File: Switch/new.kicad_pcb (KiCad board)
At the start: 2 copper layers, 53.5 x 53 mm, 9 parts, among them J1 RJ45, J2 RJ45, J3 RJ45, J4 RJ45, SW1 Driver/Auton, SW2 Enable/Disable, SW3 Pin7, SW4 Pin4, SW5 Pin1

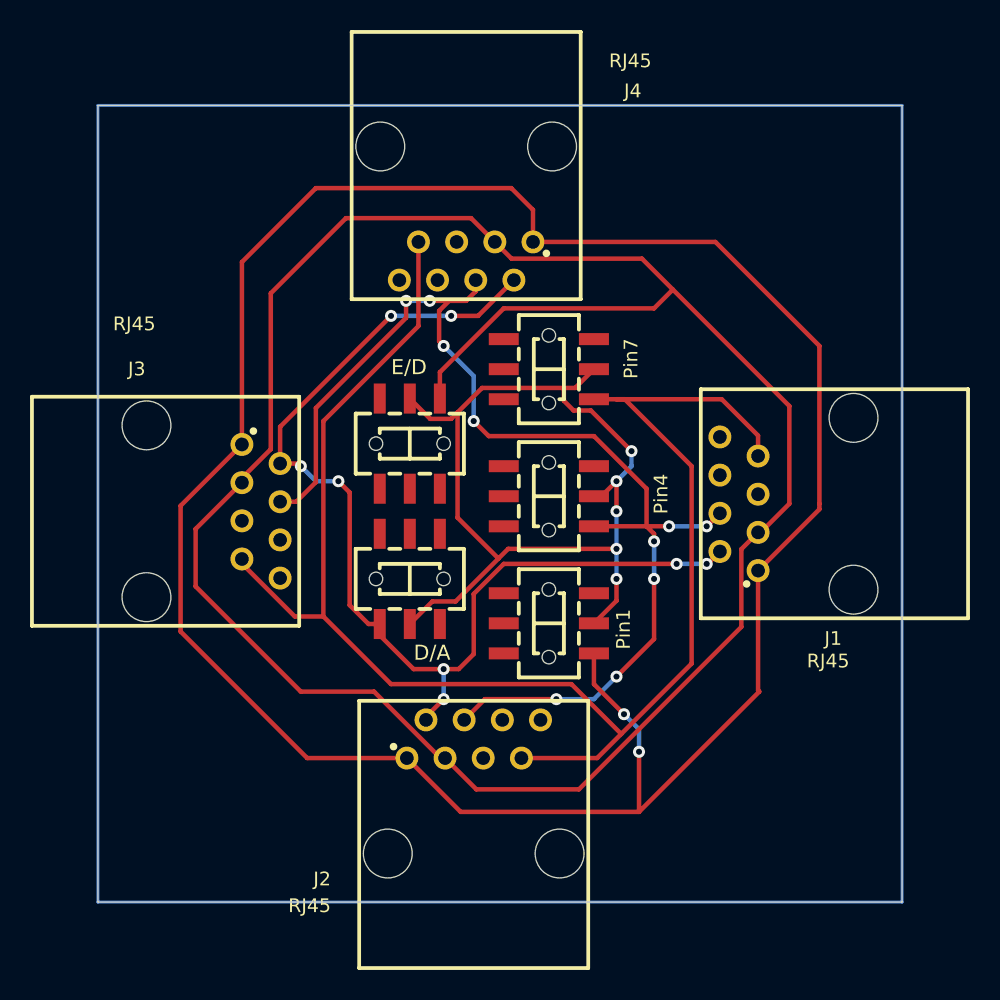
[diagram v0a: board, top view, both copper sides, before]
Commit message: switch with all files found in the folder
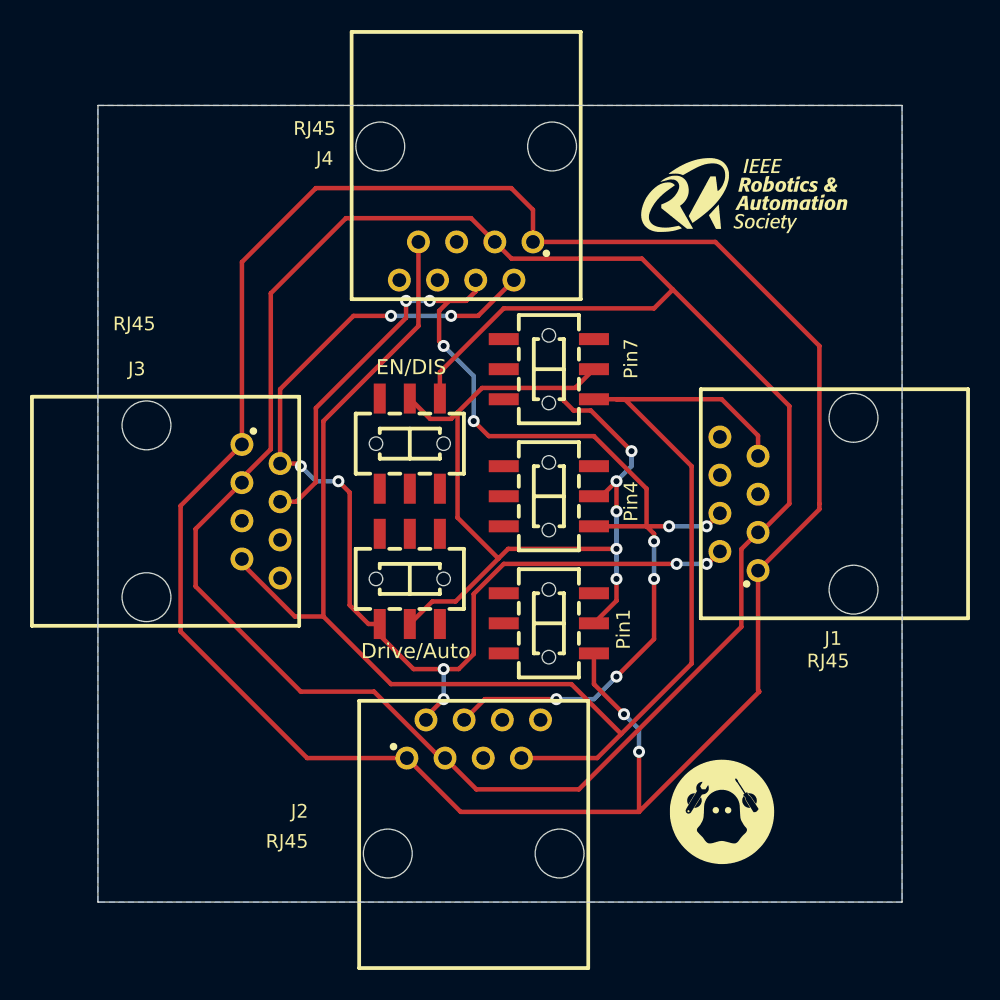
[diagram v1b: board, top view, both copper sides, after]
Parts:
- added G***: LOGO, ghost:ghost, F.Cu at (175.0, 106.5)
- added G***: LOGO, ghost:ieee, F.Cu at (176.5, 65.5)
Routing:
- net Net-(J1-Pad2): track 71.3 -> 72.7 mm
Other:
- board text added: "Drive/Auto"
- board text added: "EN/DIS"
- board text removed: "D/A"
- board text removed: "E/D"

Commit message: finalize comp switch
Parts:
- added G***: LOGO, ghost:ieee, B.Cu at (160.4, 77.4)
- added G***: LOGO, ghost:ghost, B.Cu at (160.5, 93.0)
- J1, J2, J3, J4: footprint RJ45Connector:RJ45-TH_RC0139 -> ghost:RJ45-TH_RC0139
- SW1, SW2, SW3, SW4, SW5: footprint Library:SW-SMD_MS-22D28-G020 -> ghost:SW-SMD_MS-22D28-G020
- moved G*** 18.9 mm to (179.0, 88.0)
- moved G*** 17.5 mm to (159.0, 66.5)
- moved J3 12.4 mm to (149.7, 97.7), turned to 135 degrees
- moved J2 12.3 mm to (170.4, 98.4), turned to -135 degrees
- moved J4 12.3 mm to (147.5, 76.3), turned to 45 degrees
- moved J1 12.0 mm to (171.8, 74.8), turned to -45 degrees
- moved SW3 6.99 mm to (156.5, 77.5), turned to -45 degrees
- moved SW5 6.74 mm to (168.5, 89.4), turned to -45 degrees
- moved SW1 6.28 mm to (159.8, 93.9), turned to -135 degrees
- moved SW2 5.55 mm to (153.5, 87.5), turned to 45 degrees
- moved SW4 2.30 mm to (162.5, 83.4), turned to -45 degrees
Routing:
- net Net-(J1-Pad1): track 155.6 -> 153.7 mm
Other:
- board size 53.5 x 53 mm -> 48 x 47.5 mm
- board text added: "VEXU GHOST"
- board text added: "VRC Comp Switch"
